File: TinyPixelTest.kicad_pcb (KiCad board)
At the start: 2 copper layers, 50 x 50 mm, 40 parts, among them IC1 ATTINY2313-S

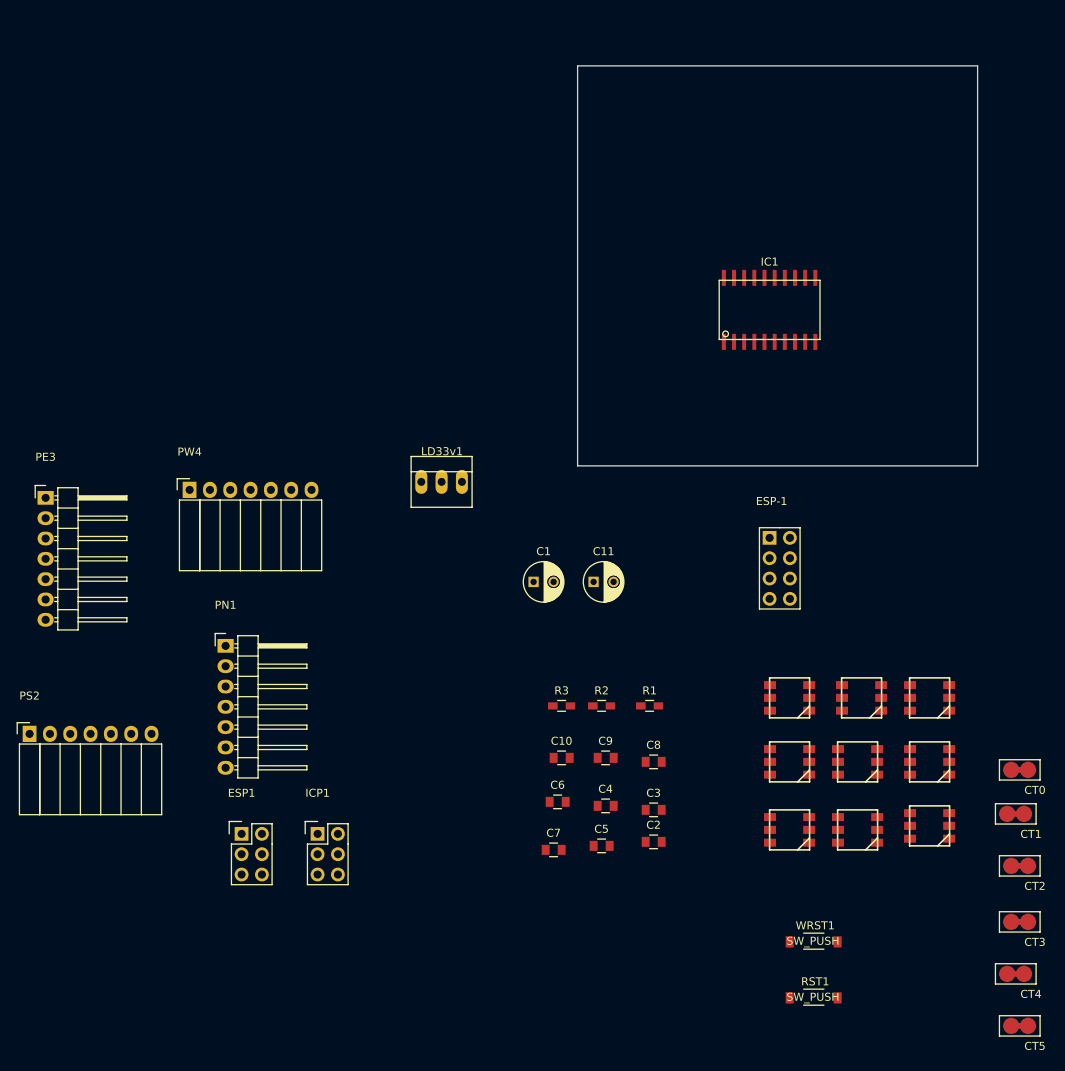
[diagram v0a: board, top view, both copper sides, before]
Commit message: Layout
Put components on board.
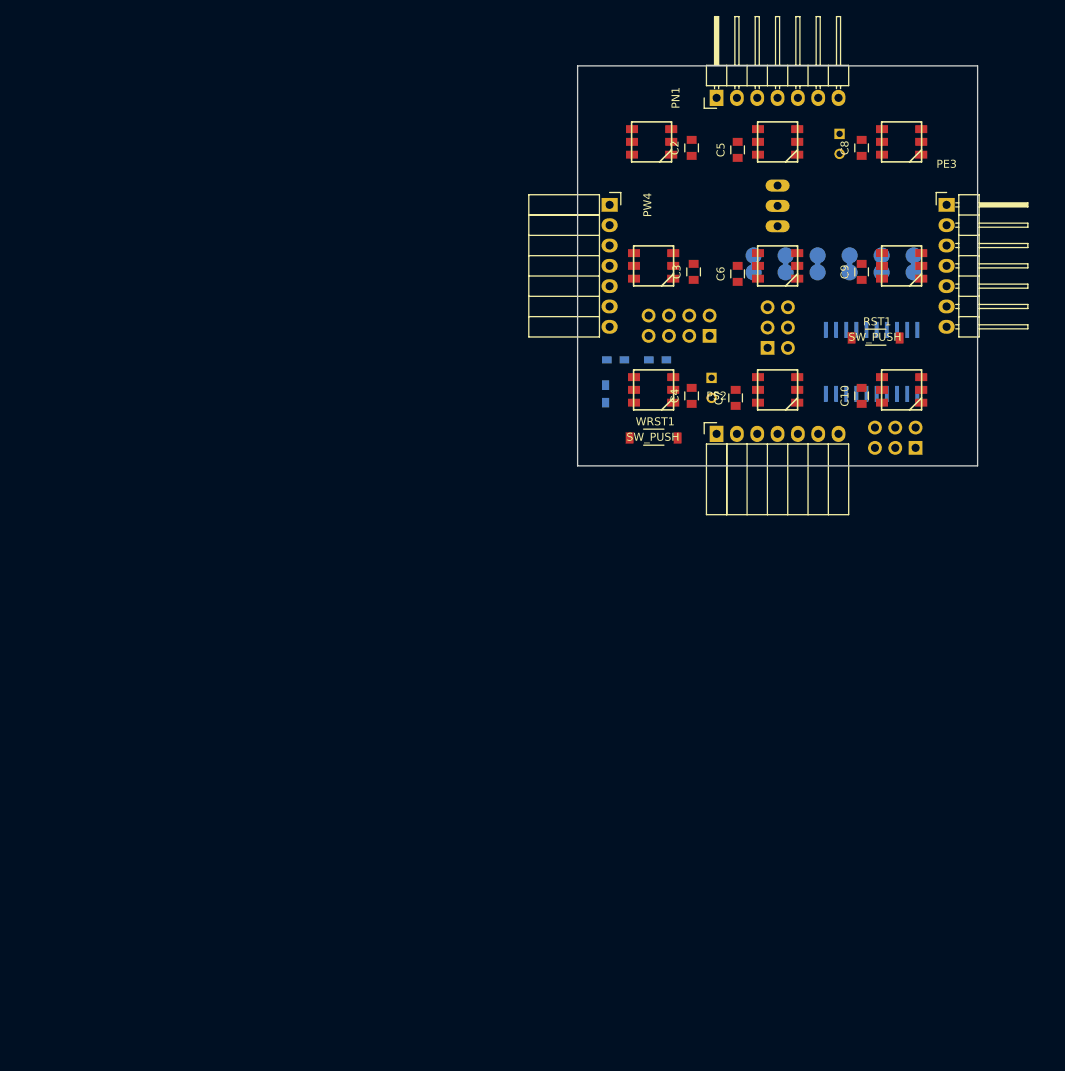
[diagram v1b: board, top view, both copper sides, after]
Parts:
- C1, C11, CT0, CT1, CT2, CT3, CT4, CT5, ESP-1, ESP1, IC1, ICP1, LD33v1, R1, R2, R3: moved to B.Cu
- moved PE3 118.4 mm to (161.1, 92.4)
- moved CT5 99.3 mm to (137.0, 101.0), turned to 90 degrees
- moved PS2 93.7 mm to (132.4, 121.0)
- moved PN1 92.0 mm to (132.4, 79.0), turned to 90 degrees
- moved CT4 91.7 mm to (141.0, 101.0), turned to 90 degrees
- moved LED-1 89.8 mm to (124.2, 84.5)
- moved ESP1 89.5 mm to (138.8, 110.2)
- moved ICP1 89.0 mm to (157.2, 122.8), turned to 90 degrees
- moved C5 88.6 mm to (135.0, 85.5), turned to 90 degrees
- moved C2 86.9 mm to (129.2, 85.2), turned to 90 degrees
- moved CT3 84.5 mm to (145.0, 101.0), turned to 90 degrees
- moved RST1 82.9 mm to (149.2, 109.0)
- moved C8 81.0 mm to (150.5, 85.2), turned to 90 degrees
- moved CT2 76.7 mm to (149.0, 101.0), turned to 90 degrees
- moved LED-2 72.5 mm to (124.5, 100.0)
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
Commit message: Tweaked pin header 3d model
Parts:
- CT0, CT1, CT2, CT3, CT4, CT5: footprint CutAway:Pin_Header_Straight_1x02 -> CutAway:CutAway1x2

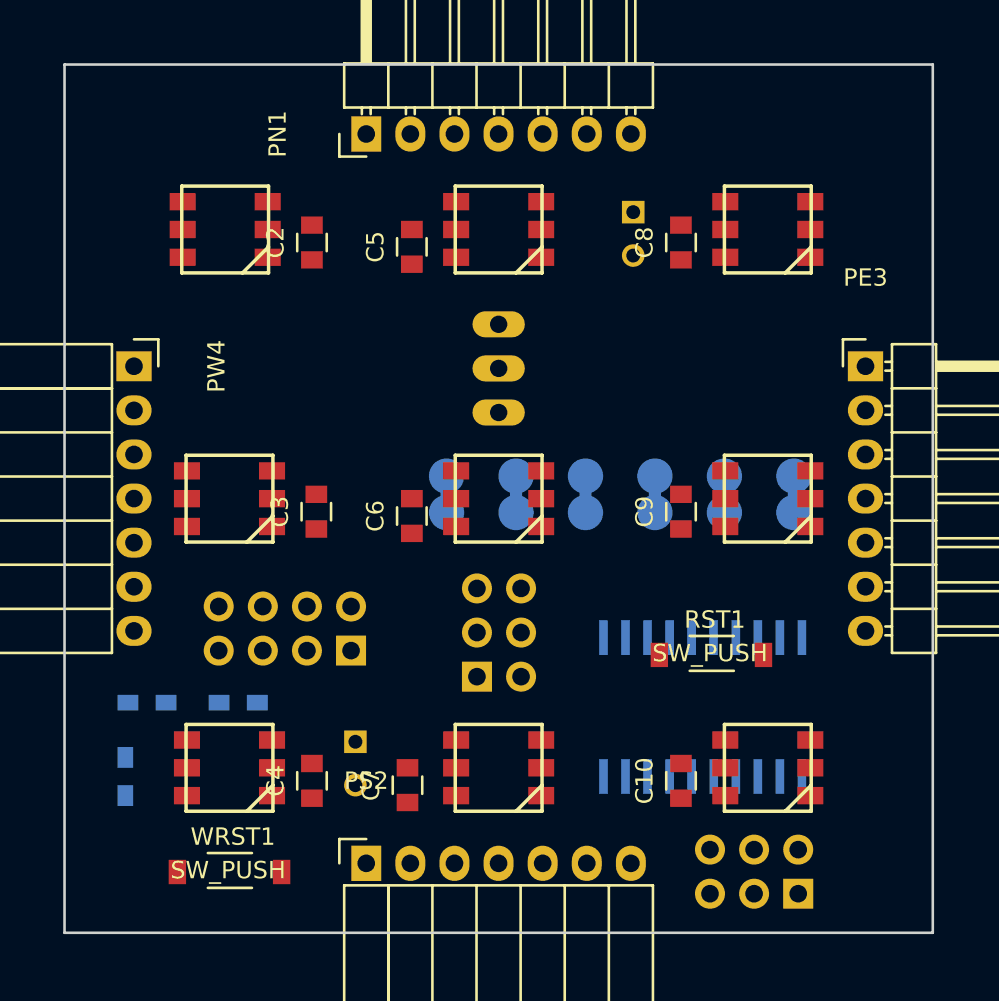
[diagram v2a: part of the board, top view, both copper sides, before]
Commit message: Attempted to route
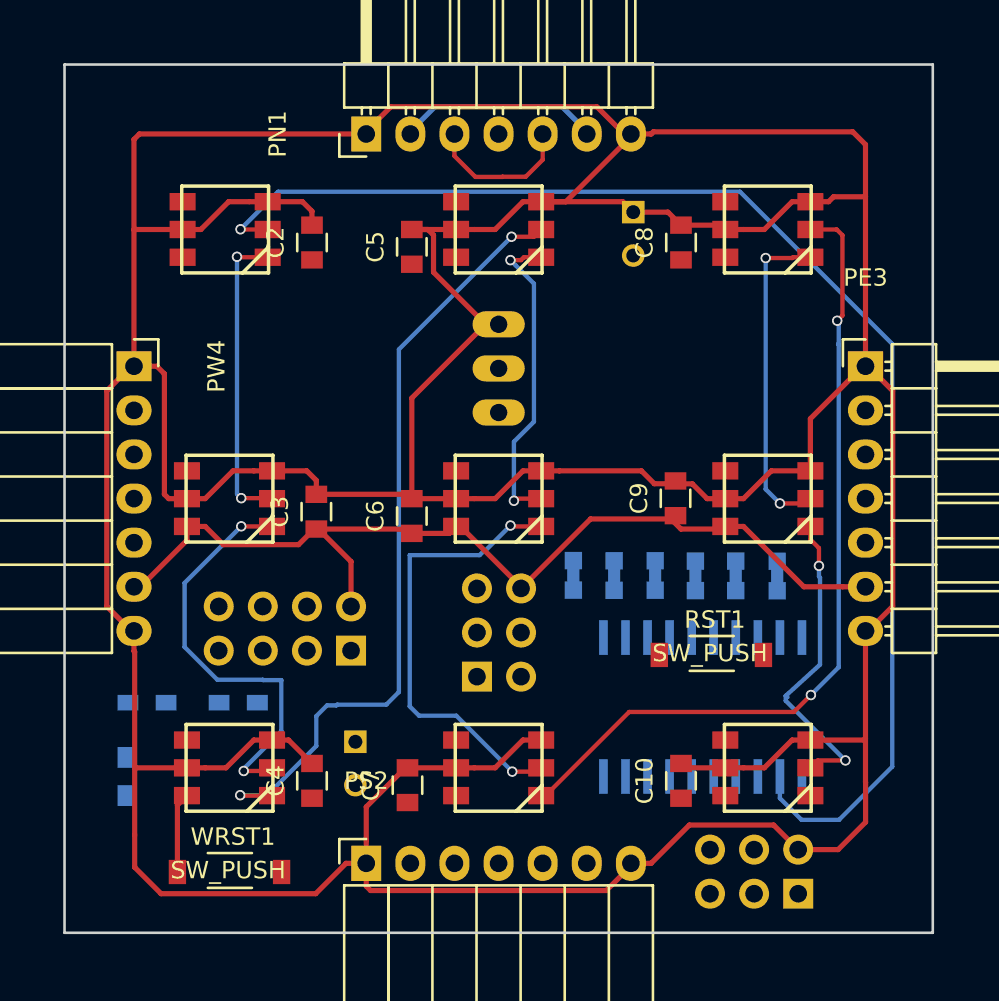
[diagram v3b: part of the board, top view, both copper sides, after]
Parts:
- moved CT5 8.67 mm to (144.3, 105.7)
- moved CT4 7.33 mm to (146.6, 105.7)
- moved CT3 6.16 mm to (149.0, 105.7)
- moved CT2 5.24 mm to (151.3, 105.7)
- moved CT0 4.80 mm to (156.0, 105.7)
- moved CT1 4.74 mm to (153.6, 105.7)
- moved C9 0.83 mm to (150.2, 100.0)
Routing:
- net +5V: track 0.00 -> 338.2 mm
- net Net-(IC1-Pad12): track 0.00 -> 77.5 mm, vias 0 -> 1
- net GND: track 0.00 -> 71.7 mm
- net Net-(LED-6-Pad1): track 0.00 -> 47.3 mm, vias 0 -> 2
- net Net-(LED-3-Pad1): track 0.00 -> 45.2 mm, vias 0 -> 2
- net Net-(LED-5-Pad1): track 0.00 -> 26.2 mm, vias 0 -> 2
- net Net-(LED-2-Pad1): track 0.00 -> 24.3 mm, vias 0 -> 2
- net Net-(LED-7-Pad1): track 0.00 -> 18.9 mm, vias 0 -> 2
- net Net-(LED-4-Pad1): track 0.00 -> 18.4 mm, vias 0 -> 2
- net Net-(LED-8-Pad1): track 0.00 -> 18.3 mm, vias 0 -> 2
- net Net-(LED-1-Pad1): track 0.00 -> 17.6 mm, vias 0 -> 2
- net Net-(ESP1-Pad2): track 0.00 -> 8.74 mm
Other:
- net class POWAR added: clearance 0.4, trace_width 0.3, via_dia 0.6, via_drill 0.4

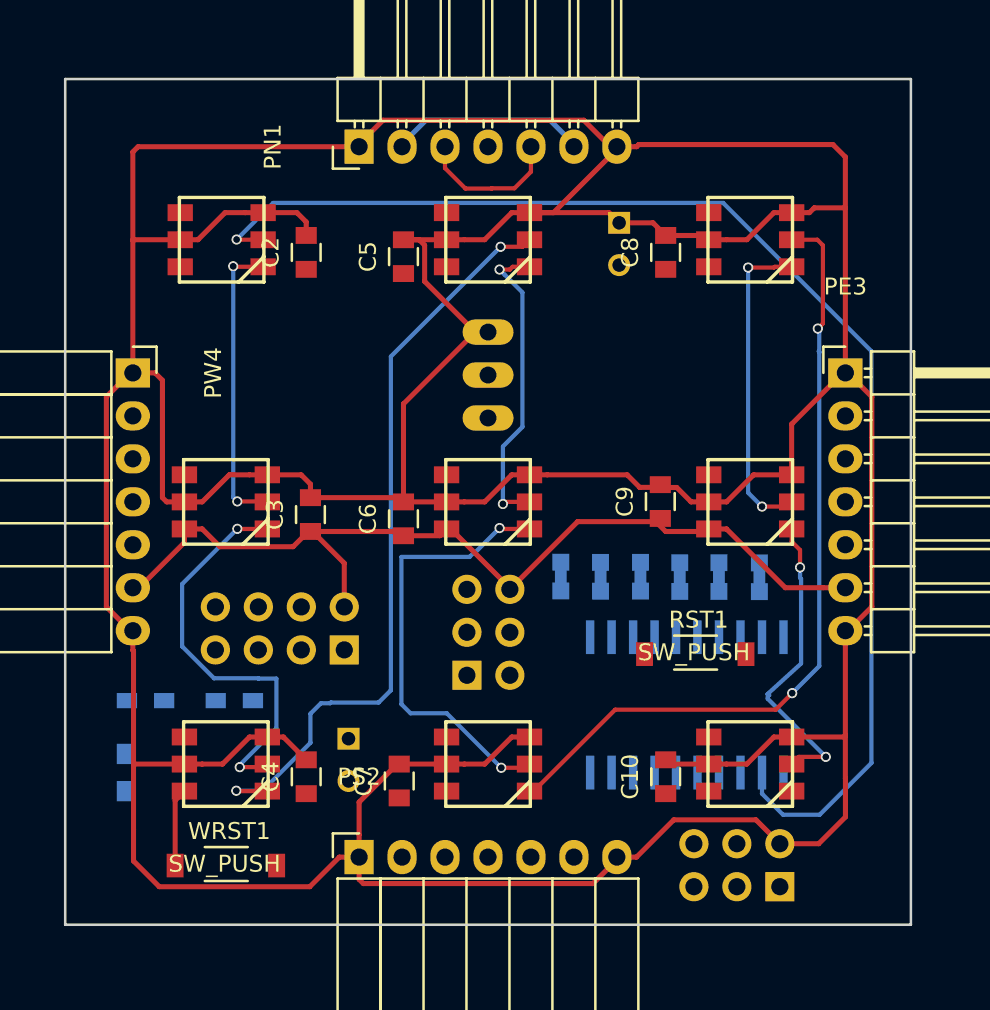
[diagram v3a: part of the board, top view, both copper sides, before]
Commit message: Added autorouted paths
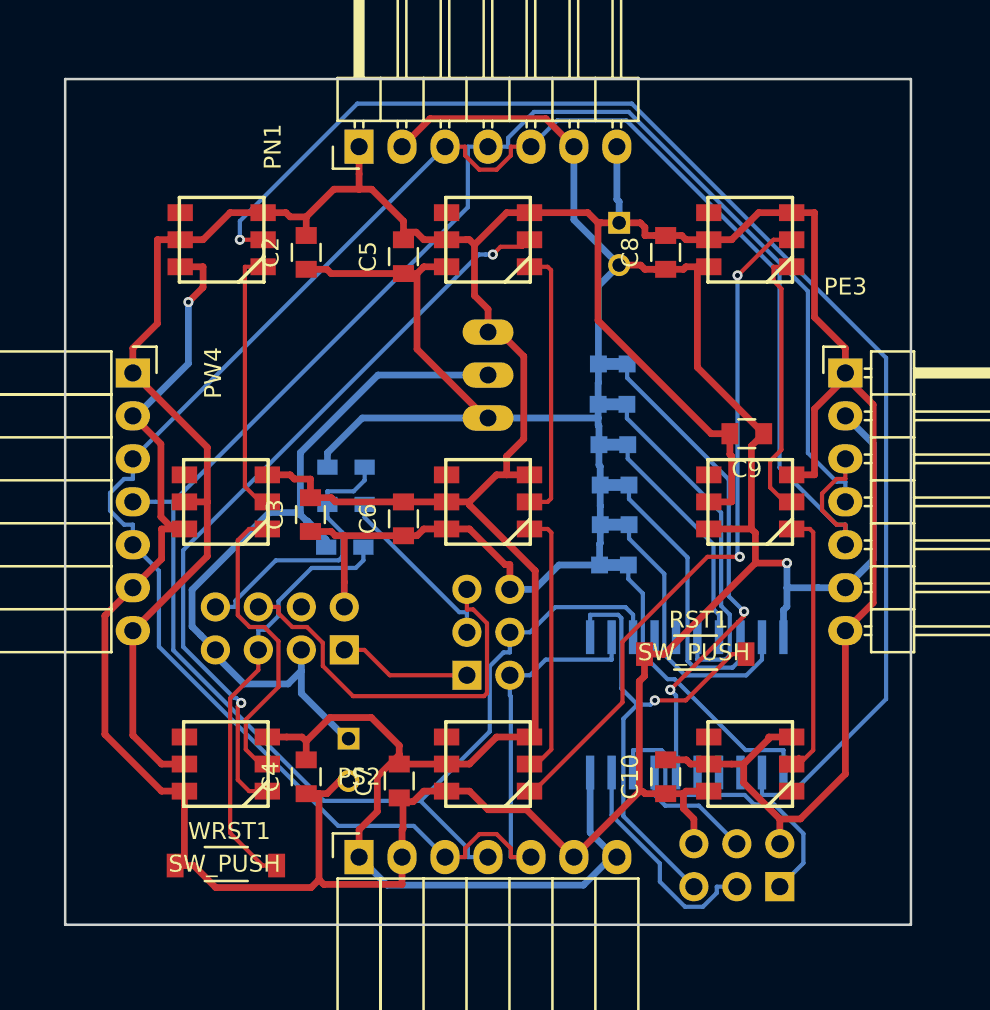
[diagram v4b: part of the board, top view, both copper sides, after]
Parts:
- moved R3 22.3 mm to (131.6, 97.9), turned to 180 degrees
- moved R2 16.6 mm to (131.6, 100.2), turned to 180 degrees
- moved CT0 15.7 mm to (148.6, 91.8), turned to 180 degrees
- moved CT1 12.5 mm to (148.6, 94.2), turned to 180 degrees
- moved R1 11.2 mm to (131.5, 102.7)
- moved CT2 9.46 mm to (148.7, 96.6), turned to 180 degrees
- moved CT3 6.68 mm to (148.7, 99.0), turned to 180 degrees
- moved C9 6.50 mm to (155.3, 96.0), turned to 180 degrees
- moved CT4 4.81 mm to (148.7, 101.3), turned to 180 degrees
- moved CT5 4.80 mm to (148.7, 103.7), turned to 180 degrees
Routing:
- net GND: track 71.7 -> 262.3 mm, vias 0 -> 2
- net Net-(ESP1-Pad2): track 8.74 -> 138.8 mm
- net Net-(ESP1-Pad4): track 0.00 -> 124.5 mm
- net +5V: track 338.2 -> 273.4 mm
- net Net-(C1-Pad1): track 0.00 -> 44.6 mm
- net Net-(IC1-Pad1): track 0.00 -> 29.3 mm, vias 0 -> 1
- net Net-(CT0-Pad1): track 0.00 -> 29.0 mm, vias 0 -> 2
- net Net-(ESP-1-Pad5): track 0.00 -> 25.4 mm
- net Net-(ESP-1-Pad6): track 0.00 -> 23.6 mm
- net Net-(CT1-Pad1): track 0.00 -> 20.7 mm
- net Net-(IC1-Pad18): track 0.00 -> 18.4 mm
- net Net-(CT5-Pad1): track 0.00 -> 17.6 mm
- net Net-(CT3-Pad1): track 0.00 -> 16.7 mm
- net Net-(CT4-Pad1): track 0.00 -> 16.5 mm
- net Net-(ESP-1-Pad8): track 0.00 -> 16.4 mm
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
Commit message: Final v0.1 !
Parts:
- renumbered RST1 to RST, WRST1 to WRST
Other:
- board text added: "+5v MOSI GND"
- board text added: "GP0"
- board text added: "MISO"
- board text added: "RST"
- board text added: "TinyPixels 3x3 v0.1 Mike Rockwood Joseph Duchesne"
- board text added: "WRX"
- board text added: "WTX"
